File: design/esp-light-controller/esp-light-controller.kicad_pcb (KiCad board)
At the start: 2 copper layers, 26.7 x 33 mm, 7 parts, among them J1 WS2812b, J2 USB, Q1 2N7000, U1 LD1117V33, U2 ESP-01v090

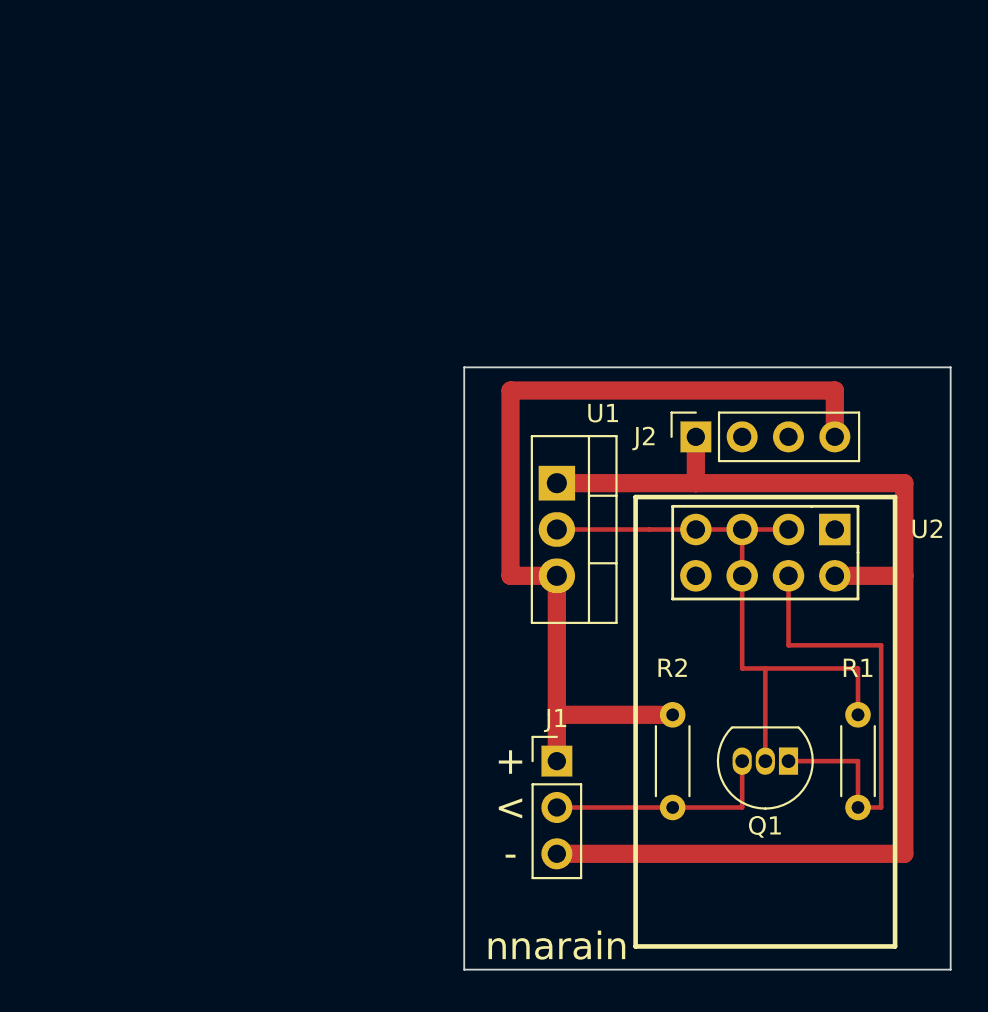
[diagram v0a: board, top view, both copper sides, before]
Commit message: Update to surface mount components
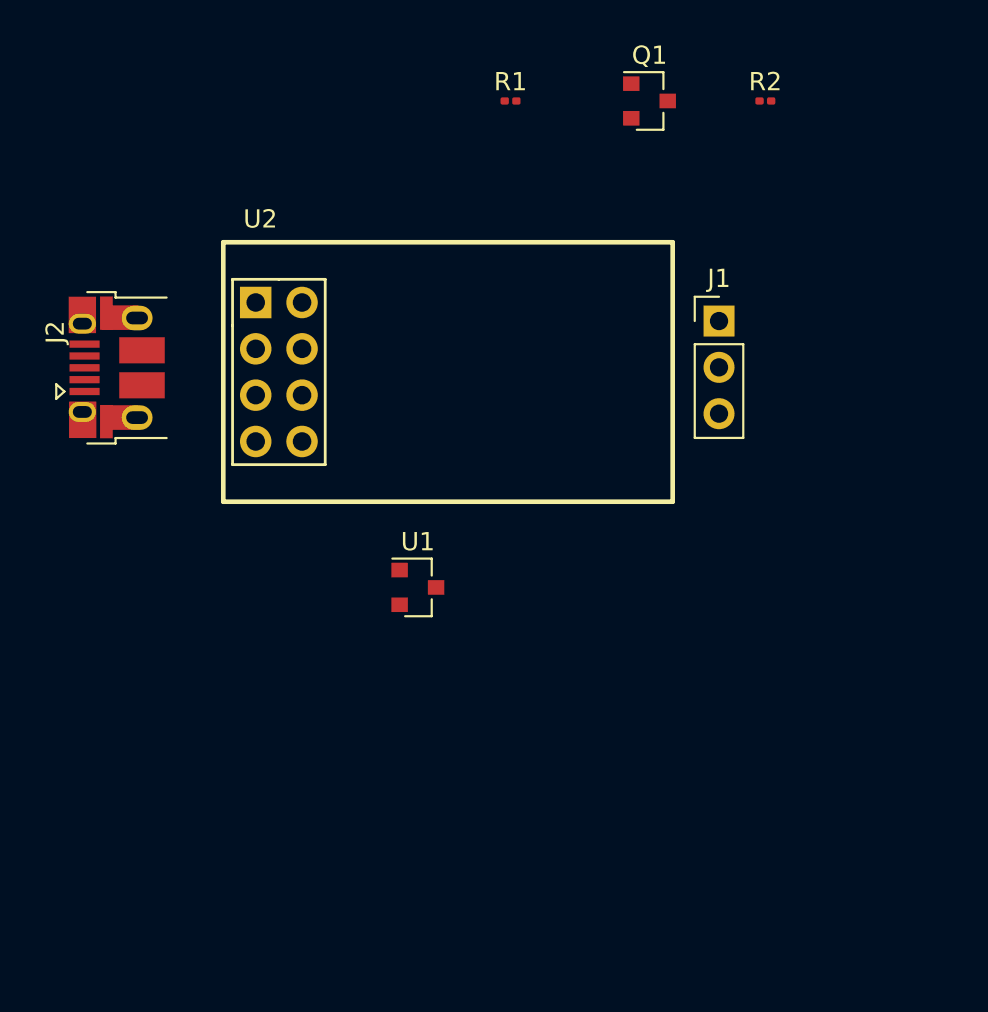
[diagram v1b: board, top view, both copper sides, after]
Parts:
- J2: value USB -> USB_B_Micro; footprint Connector_PinSocket_2.54mm:PinSocket_1x04_P2.54mm_Vertical -> Connector_USB:USB_Micro-B_Amphenol_10103594-0001LF_Horizontal
- Q1: value 2N7000 -> 2N7002; footprint Package_TO_SOT_THT:TO-92_Inline -> Package_TO_SOT_SMD:SOT-23
- R1, R2: footprint Resistor_THT:R_Axial_DIN0204_L3.6mm_D1.6mm_P5.08mm_Horizontal -> Resistor_SMD:R_0201_0603Metric
- U1: value LD1117V33 -> AP2138; footprint Package_TO_SOT_THT:TO-220-3_Vertical -> Package_TO_SOT_SMD:SOT-23
- moved R1 38.7 mm to (139.7, 62.9), turned to 0 degrees
- moved Q1 37.0 mm to (147.3, 62.9), turned to 0 degrees
- moved U2 34.1 mm to (125.7, 73.9), turned to 0 degrees
- moved R2 34.0 mm to (153.7, 62.9), turned to 0 degrees
- moved J2 32.0 mm to (118.1, 77.5)
- moved J1 25.7 mm to (151.1, 74.9)
- moved U1 9.53 mm to (134.6, 89.5), turned to 0 degrees
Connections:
- J2 pad 1: GND -> +5V
- J2 pad 4: +5V -> GND
- Q1 pad 1: Net-(Q1-Pad1) -> +3V3
- Q1 pad 2: +3V3 -> Net-(Q1-Pad2)
- R1 pad 2: Net-(Q1-Pad1) -> Net-(Q1-Pad2)
- U2 pad 4: Net-(Q1-Pad1) -> Net-(Q1-Pad2)
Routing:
- net GND: track 64.8 -> 0.00 mm
- net +5V: track 49.5 -> 0.00 mm
- net +3V3: track 34.3 -> 0.00 mm
- net Net-(Q1-Pad1): track 25.4 -> 0.00 mm
- net Net-(J1-Pad2): track 12.7 -> 0.00 mm
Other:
- board outline removed
- board text removed: "+"
- board text removed: "-"
- board text removed: "<"
- board text removed: "nnarain"

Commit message: Version 2 design
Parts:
- added G***: LOGO, symbols:logo-bsilk, F.Cu at (133.3, 77.5)
- added J3: Serial, Connector_PinHeader_2.54mm:PinHeader_1x02_P2.54mm_Vertical, F.Cu at (121.9, 71.8)
- J1: footprint Connector_PinHeader_2.54mm:PinHeader_1x03_P2.54mm_Vertical -> Connector_JST:JST_XH_S3B-XH-A_1x03_P2.50mm_Horizontal
- J2: footprint Connector_USB:USB_Micro-B_Amphenol_10103594-0001LF_Horizontal -> digikey-footprints:USB_Micro_B_Female_1050170001
- moved R2 25.6 mm to (134.6, 80.0), turned to 180 degrees
- moved Q1 20.7 mm to (132.7, 77.5)
- moved R1 13.1 mm to (134.6, 74.9), turned to 180 degrees
- moved J1 12.5 mm to (139.7, 80.0), turned to 90 degrees
- moved U1 6.84 mm to (132.1, 83.2), turned to 180 degrees
- moved J2 4.49 mm to (122.6, 78.1), turned to 270 degrees
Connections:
- J1 pad 1: +5V -> GND
- J1 pad 3: GND -> +5V
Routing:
- net GND: track 0.00 -> 53.2 mm
- net +5V: track 0.00 -> 33.6 mm
- net +3V3: track 0.00 -> 24.1 mm
- net Net-(J3-Pad1): track 0.00 -> 19.4 mm
- net Net-(J3-Pad2): track 0.00 -> 11.0 mm
- net Net-(J1-Pad2): track 0.00 -> 9.64 mm
- net Net-(Q1-Pad2): track 0.00 -> 9.63 mm
- net (no net): track 0.00 -> 5.50 mm
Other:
- board outline added: 31.8 x 15.9 mm
- board text added: "+ > -"
- board text added: "esp-lights v2"
- board text added: "nnarain"

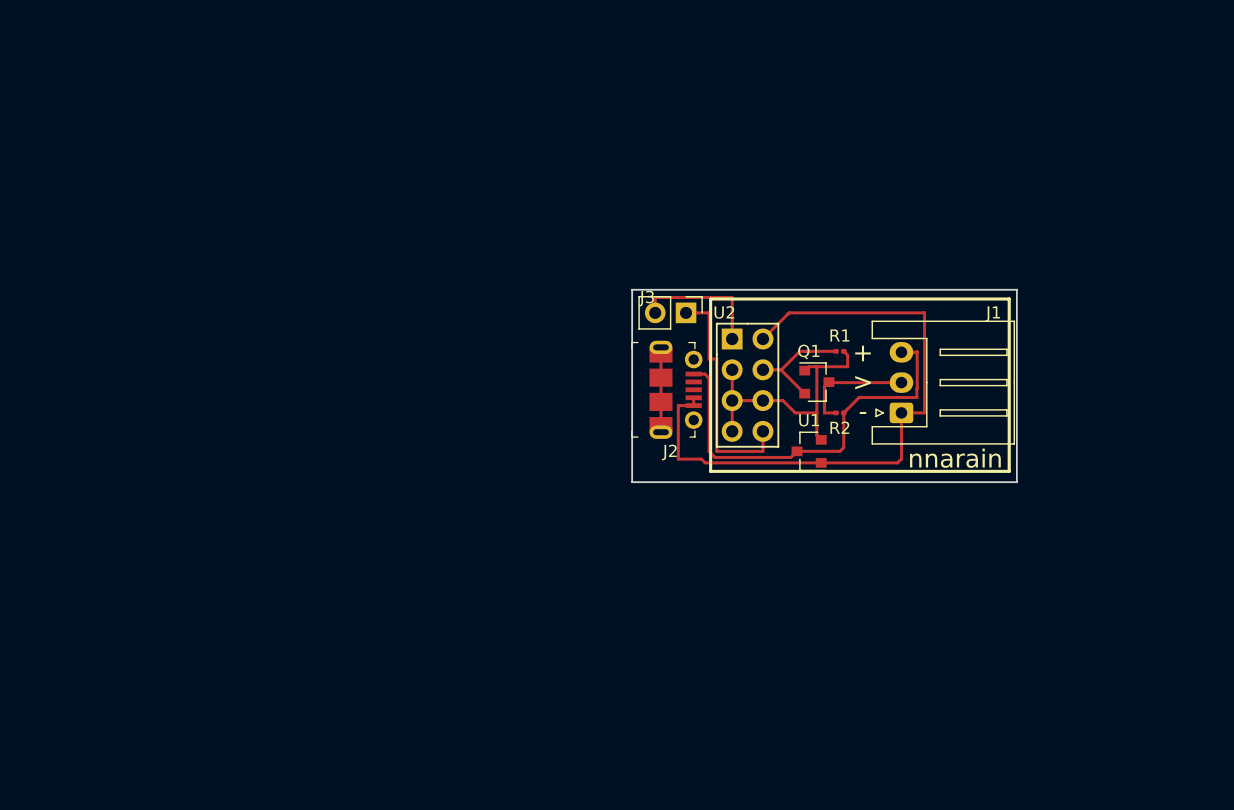
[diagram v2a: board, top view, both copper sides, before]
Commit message: ESP32 based design
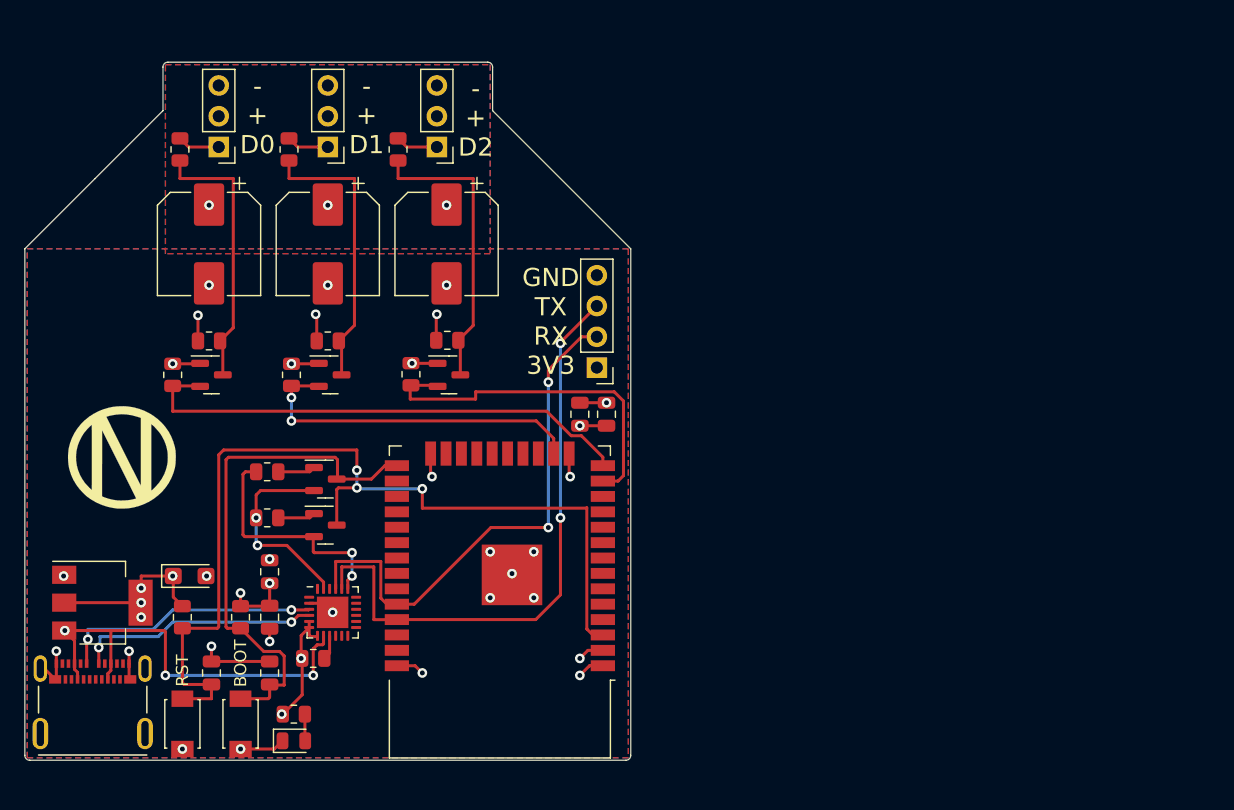
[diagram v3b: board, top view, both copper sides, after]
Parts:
- removed the G*** at (133.3, 77.5)
- added C1: 1uF, Capacitor_SMD:C_0805_2012Metric, F.Cu at (87.6, 93.1)
- added C10: 1000uF, Capacitor_SMD:CP_Elec_8x10, F.Cu at (82.6, 66.1)
- added C2: 100nF, Capacitor_SMD:C_0805_2012Metric, F.Cu at (87.6, 96.9)
- added C3: 10uF, Capacitor_SMD:C_0805_2012Metric, F.Cu at (115.4, 80.1)
- added C4: 22uF, Capacitor_Tantalum_SMD:CP_EIA-3216-18_Kemet-A, F.Cu at (81.0, 93.5)
- added C5: 100nF, Capacitor_SMD:C_0805_2012Metric, F.Cu at (113.2, 80.1)
- added C6: 100nF, Capacitor_SMD:C_0805_2012Metric, F.Cu at (82.8, 101.5)
- added C7: 100nF, Capacitor_SMD:C_0805_2012Metric, F.Cu at (87.6, 101.5)
- added C8: 1000uF, Capacitor_SMD:CP_Elec_8x10, F.Cu at (102.2, 66.1)
- added C9: 1000uF, Capacitor_SMD:CP_Elec_8x10, F.Cu at (92.4, 66.1)
- added D1: PWR, LED_SMD:LED_0805_2012Metric, F.Cu at (89.6, 107.1)
- added G***: LOGO, symbols:logo, F.Cu at (75.4, 83.7)
- added J4: UART, Connector_PinHeader_2.54mm:PinHeader_1x04_P2.54mm_Vertical, F.Cu at (114.6, 76.3)
- added P1: USB_C_Plug_USB2.0, ki-usb-connectors:MOLEX_105450-0101, F.Cu at (73.0, 104.5)
- added Q2: 2N7002, Package_TO_SOT_SMD:SOT-23, F.Cu at (82.8, 76.9)
- added Q3: 2N7002, Package_TO_SOT_SMD:SOT-23, F.Cu at (92.6, 76.9)
- added Q4: 2N7002, Package_TO_SOT_SMD:SOT-23, F.Cu at (92.2, 89.3)
- added Q5: 2N7002, Package_TO_SOT_SMD:SOT-23, F.Cu at (92.2, 85.5)
- added R10: 10k, Resistor_SMD:R_0805_2012Metric, F.Cu at (92.4, 74.1)
- added R11: 10k, Resistor_SMD:R_0805_2012Metric, F.Cu at (87.4, 88.7)
- added R12: 10k, Resistor_SMD:R_0805_2012Metric, F.Cu at (87.4, 84.9)
- added R13: 100, Resistor_SMD:R_0805_2012Metric, F.Cu at (80.2, 58.3)
- added R14: 100, Resistor_SMD:R_0805_2012Metric, F.Cu at (89.2, 58.3)
- added R15: 100, Resistor_SMD:R_0805_2012Metric, F.Cu at (98.2, 58.3)
- added R3: 10k, Resistor_SMD:R_0805_2012Metric, F.Cu at (99.2, 76.8)
- added R4: 10k, Resistor_SMD:R_0805_2012Metric, F.Cu at (79.6, 76.9)
- added R5: 10k, Resistor_SMD:R_0805_2012Metric, F.Cu at (80.4, 96.9)
- added R6: 10k, Resistor_SMD:R_0805_2012Metric, F.Cu at (102.2, 74.0)
- added R7: 10k, Resistor_SMD:R_0805_2012Metric, F.Cu at (82.6, 74.1)
- added R8: 10k, Resistor_SMD:R_0805_2012Metric, F.Cu at (85.2, 96.9)
- added R9: 10k, Resistor_SMD:R_0805_2012Metric, F.Cu at (89.4, 76.9)
- added SW1: RST, tactile_switches:TS-1088-AR02016, F.Cu at (80.4, 105.7)
- added SW2: BOOT, tactile_switches:TS-1088-AR02016, F.Cu at (85.2, 105.7)
- added U3: ESP32-WROOM-32, RF_Module:ESP32-WROOM-32, F.Cu at (106.6, 92.6)
- J1: value WS2812b -> LED0; footprint Connector_JST:JST_XH_S3B-XH-A_1x03_P2.50mm_Horizontal -> Connector_PinHeader_2.54mm:PinHeader_1x03_P2.54mm_Vertical
- J2: value USB_B_Micro -> LED1; footprint digikey-footprints:USB_Micro_B_Female_1050170001 -> Connector_PinHeader_2.54mm:PinHeader_1x03_P2.54mm_Vertical
- J3: value Serial -> LED2; footprint Connector_PinHeader_2.54mm:PinHeader_1x02_P2.54mm_Vertical -> Connector_PinHeader_2.54mm:PinHeader_1x03_P2.54mm_Vertical
- R1: value 10k -> 4.7k; footprint Resistor_SMD:R_0201_0603Metric -> Resistor_SMD:R_0805_2012Metric
- R2: value 10k -> 330; footprint Resistor_SMD:R_0201_0603Metric -> Resistor_SMD:R_0805_2012Metric
- U1: value AP2138 -> CP2104; footprint Package_TO_SOT_SMD:SOT-23 -> Package_DFN_QFN:QFN-24-1EP_4x4mm_P0.5mm_EP2.6x2.6mm
- U2: value ESP-01v090 -> AMS1117-3.3; footprint kicad-ESP8266:ESP-01 -> Package_TO_SOT_SMD:SOT-223-3_TabPin2
- moved J1 60.5 mm to (83.4, 58.1), turned to 180 degrees
- moved U2 56.3 mm to (73.8, 95.7)
- moved R2 51.5 mm to (89.6, 104.9), turned to 0 degrees
- moved R1 50.3 mm to (91.2, 100.3), turned to 0 degrees
- moved U1 41.5 mm to (92.8, 96.5), turned to 0 degrees
- moved J2 36.2 mm to (92.4, 58.1), turned to 180 degrees
- moved Q1 30.4 mm to (102.4, 76.9)
- moved J3 24.7 mm to (101.4, 58.1), turned to 180 degrees
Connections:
- J1 pad 1: GND -> Net-(J1-Pad1)
- J1 pad 2: Net-(J1-Pad2) -> +5V
- J1 pad 3: +5V -> GND
- J2 pad 1: +5V -> Net-(J2-Pad1)
- J2 pad 2: Net-(J2-Pad2) -> +5V
- J2 pad 3: Net-(J2-Pad3) -> GND
- J3 pad 2: Net-(J3-Pad2) -> +5V
- Q1 pad 2: Net-(Q1-Pad2) -> /ledctl2
- Q1 pad 3: Net-(J1-Pad2) -> /led2
- R1 pad 2: Net-(Q1-Pad2) -> Net-(R1-Pad2)
- R2 pad 1: +5V -> +3V3
- R2 pad 2: Net-(J1-Pad2) -> Net-(D1-Pad2)
- U1 pad 1: GND -> unconnected-(U1-Pad1)
- U1 pad 2: +3V3 -> GND
- U1 pad 3: +5V -> /usb_dp
- U2 pad 1: Net-(J3-Pad2) -> GND
- U2 pad 2: GND -> +3V3
- U2 pad 3: +3V3 -> +5V
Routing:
- net /en: track 0.00 -> 79.3 mm, vias 0 -> 3
- net /esp_tx: track 0.00 -> 50.1 mm, vias 0 -> 2
- net /esp_rx: track 0.00 -> 43.8 mm, vias 0 -> 2
- net /io0: track 0.00 -> 43.1 mm
- net /ledctl0: track 0.00 -> 42.1 mm
- net /ledctl2: track 0.00 -> 30.0 mm
- net /ledctl1: track 0.00 -> 28.7 mm, vias 0 -> 2
- net /led2: track 0.00 -> 24.5 mm
- net /led1: track 0.00 -> 23.7 mm
- net GND: track 53.2 -> 29.9 mm, vias 0 -> 23
- net /led0: track 0.00 -> 22.6 mm
- net /usb_dp: track 0.00 -> 21.9 mm, vias 0 -> 2
- net /usb_dm: track 0.00 -> 20.3 mm, vias 0 -> 2
- net /rts: track 0.00 -> 19.7 mm, vias 0 -> 2
- net /dtr: track 0.00 -> 16.4 mm, vias 0 -> 2
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- added copper zone on In1.Cu, net +3V3
- added copper zone on In1.Cu, net +5V
- added copper zone on B.Cu, net GND
- added copper zone on F.Cu, net GND
- added copper zone on In2.Cu, net GND
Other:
- board size 31.8 x 15.9 mm -> 50 x 57.6 mm
- copper layers 2 -> 4
- net class Default removed
- board text added: "- + D0"
- board text added: "- + D1"
- board text added: "- + D2"
- board text added: "GND TX RX 3V3"
- board text added: "esp-light-controller :: Rev C nnarain"
- board text removed: "+ > -"
- board text removed: "esp-lights v2"
- board text removed: "nnarain"

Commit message: update
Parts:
- moved C5 47.8 mm to (160.9, 77.0)
- moved C8 47.8 mm to (149.9, 63.0)
- moved Q4 47.8 mm to (139.9, 86.2)
- moved Q5 47.8 mm to (139.9, 82.4)
- moved R1 47.8 mm to (138.9, 97.2)
- moved R14 47.8 mm to (136.9, 55.2)
- moved R15 47.8 mm to (145.9, 55.2)
- moved R3 47.8 mm to (146.9, 73.7)
- moved R6 47.8 mm to (149.9, 70.9)
- moved R8 47.8 mm to (132.9, 93.8)
- moved SW2 47.8 mm to (132.9, 102.6)
- moved C3 47.8 mm to (163.1, 77.0)
- moved C4 47.8 mm to (128.7, 90.4)
- moved C6 47.8 mm to (130.5, 98.4)
- moved C9 47.8 mm to (140.1, 63.0)
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
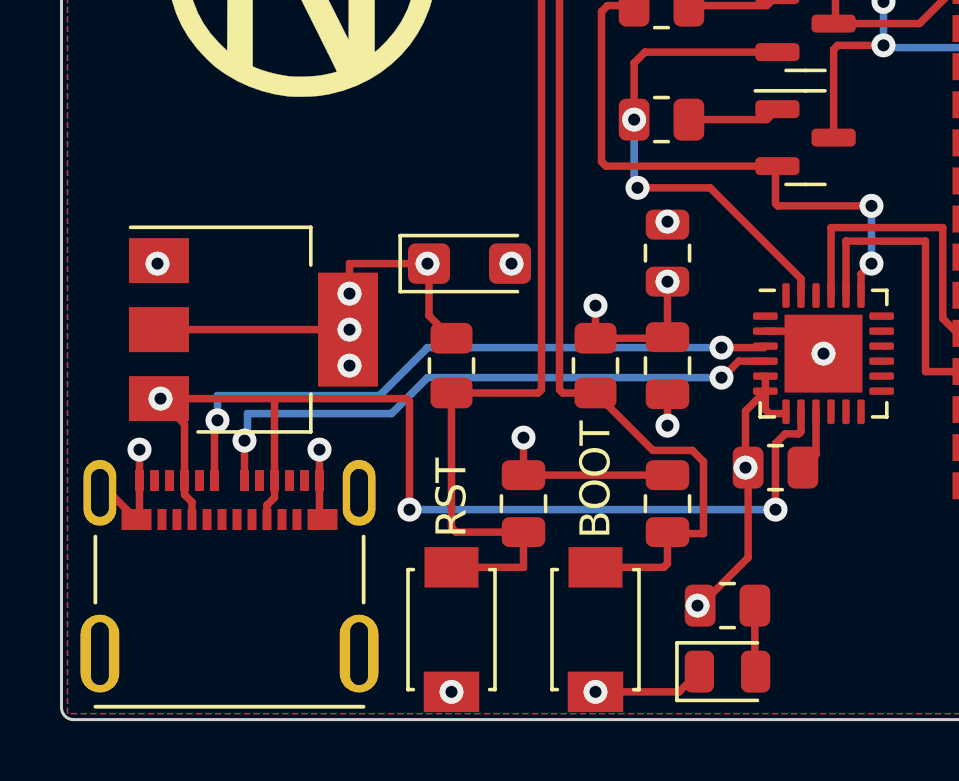
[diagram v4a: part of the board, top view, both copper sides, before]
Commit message: Resolves #38. Select USB-C Connector that works for JLCPCB assembly
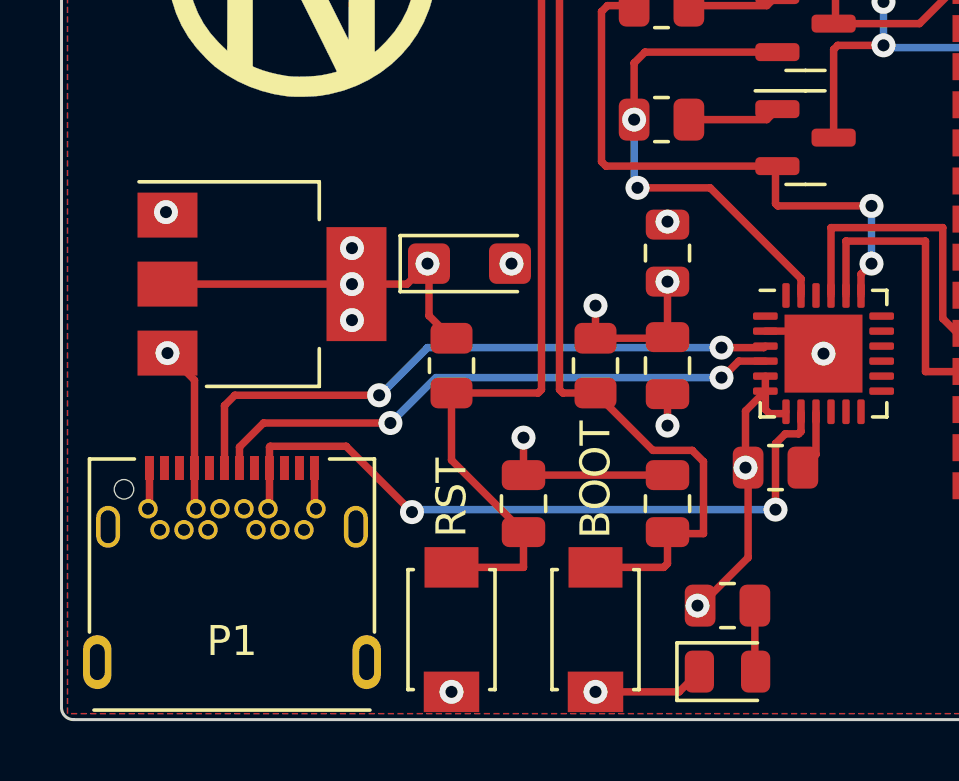
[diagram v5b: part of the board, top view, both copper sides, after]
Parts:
- P1: footprint ki-usb-connectors:MOLEX_105450-0101 -> USB-C-Connectors:TYPE-C-31-M-04
- moved U2 1.54 mm to (121.8, 91.1)
- moved P1 0.89 mm to (120.8, 102.3)
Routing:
- net +5V: track 43.2 -> 35.9 mm
- net GND: track 29.9 -> 26.5 mm, vias 23 -> 21
- net /en: track 79.3 -> 77.9 mm
- net +3V3: track 39.2 -> 38.3 mm
- net /usb_dp: track 21.9 -> 20.9 mm
- net /usb_dm: track 20.3 -> 19.4 mm
